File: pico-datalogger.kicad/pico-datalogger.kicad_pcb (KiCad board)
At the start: 2 copper layers, 21 x 33.8 mm, 18 parts, among them J1 JST-PH2 Bat, J2 Pico Pin 1-13, J3 Pico Pin 40-28, J4 Alt-Bat, SW1 SW_Push_SLIM, U1 SN74HC74N, U2 PCF8563T, Y1 Crystal

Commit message: Rev. 0.9: initial routing
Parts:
- removed C3: 22pF, Capacitor_SMD:C_0402_1005Metric
- removed D1: D_Schottky, Diode_SMD:D_SMA
- removed R5: 10K, Resistor_SMD:R_0402_1005Metric
- added BT1: Coin_Cell, user:CR2032_Holder, F.Cu at (165.0, 82.5)
- added J5: Conn_I2S, Connector_PinHeader_2.54mm:PinHeader_1x06_P2.54mm_Vertical, F.Cu at (121.2, 92.3)
- added J7: Micro_SD_TF_PUSH, user:TF-Push, F.Cu at (164.8, 127.7)
- added U3: Pico, user:RPi_Pico_TH_nodbg, F.Cu at (139.2, 94.6)
- J1: value JST-PH2 Bat -> JST-PH2 VCC
- J2: value Pico Pin 1-13 -> Conn_I2C_Internal; footprint user:Connector_1x13_no_solder -> Connector_PinHeader_2.54mm:PinHeader_2x04_P2.54mm_Vertical; moved to F.Cu
- J3: value Pico Pin 40-28 -> RFM9x_Lora_Breakout; footprint user:Connector_1x13_no_solder -> user:RFM9x_Lora_Breakout
- J4: value Alt-Bat -> Alt-VCC
- JP1: value Jmp_CLKOUT -> Jumper_VSYS; footprint Jumper:SolderJumper-2_P1.3mm_Open_Pad1.0x1.5mm -> Connector_PinHeader_2.54mm:PinHeader_1x02_P2.54mm_Vertical; moved to F.Cu
- U2: value PCF8563T -> PCF8523T
- moved J1 67.8 mm to (169.9, 103.1), turned to 90 degrees
- moved J4 62.2 mm to (162.8, 104.3), turned to 0 degrees
- moved JP1 54.0 mm to (152.4, 73.0), turned to 0 degrees
- moved C1 41.5 mm to (136.9, 87.4), turned to 90 degrees
- moved R4 40.4 mm to (133.7, 79.3), turned to 0 degrees
- moved R3 40.1 mm to (133.7, 78.0), turned to 0 degrees
- moved U2 37.6 mm to (138.6, 80.0), turned to 180 degrees
- moved R2 37.2 mm to (132.9, 95.0)
- moved U1 36.9 mm to (138.1, 92.2)
- moved R1 35.7 mm to (133.2, 83.2), turned to 180 degrees
- moved Y1 34.4 mm to (142.3, 84.0), turned to 0 degrees
- moved C2 33.0 mm to (135.9, 83.2), turned to 180 degrees
- moved J2 32.2 mm to (118.5, 67.8), turned to 0 degrees
- moved SW1 31.0 mm to (144.1, 135.3), turned to 180 degrees
- moved J3 28.6 mm to (121.8, 118.6), turned to 90 degrees
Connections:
- J2 pad 1: unconnected-(J2-Pad1) -> GND
- J2 pad 2: unconnected-(J2-Pad2) -> GND
- J2 pad 3: GND -> +3V3
- J2 pad 4: /SDA -> +3V3
- J2 pad 5: /SCL -> /SDA
- J2 pad 6: /GP4_DONE -> /SDA
- J2 pad 7: /GP5_CLKOUT -> /SCL
- J2 pad 8: GND -> /SCL
- J3 pad 1: unconnected-(J3-Pad1) -> +3V3
- J3 pad 11: unconnected-(J3-Pad11) -> (no net)
- J3 pad 12: unconnected-(J3-Pad12) -> (no net)
- J3 pad 13: GND -> (no net)
- J3 pad 2: /VSYS -> GND
- J3 pad 3: GND -> /Lora_EN
- J3 pad 4: /3V3_EN -> unconnected-(J3-Pad4)
- J3 pad 5: +3V3 -> /SCLK1
- J3 pad 6: unconnected-(J3-Pad6) -> /MISO1
- J3 pad 7: unconnected-(J3-Pad7) -> /MOSI1
- J3 pad 8: GND -> /Lora_CS
- J3 pad 9: unconnected-(J3-Pad9) -> /Lora_RST
- JP1 pad 1: /GP5_CLKOUT -> /VSYS
- JP1 pad 2: /CLKOUT -> +BATT
- R3 pad 1: /SCL -> +3V3
- R3 pad 2: +3V3 -> /SDA
- R4 pad 1: /SDA -> +3V3
- R4 pad 2: +3V3 -> /SCL
- U2 pad 3: /1~{PRE} -> Net-(BT1-Pad1)
- U2 pad 7: /CLKOUT -> /1~{PRE}
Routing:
- net +3V3: track 12.8 -> 145.5 mm, vias 1 -> 2
- net /SD_CS: track 0.00 -> 31.4 mm
- net Net-(BT1-Pad1): track 0.00 -> 30.2 mm
- net /DOUT: track 0.00 -> 27.4 mm, vias 0 -> 2
- net GND: track 27.7 -> 1.78 mm, vias 4 -> 0
- net +BATT: track 53.6 -> 77.7 mm, vias 2 -> 1
- net /MOSI0: track 0.00 -> 22.9 mm
- net /SCLK0: track 0.00 -> 19.8 mm
- net /1~{PRE}: track 49.8 -> 69.5 mm
- net /MISO0: track 0.00 -> 14.3 mm
- net /MISO1: track 0.00 -> 13.6 mm
- net /Lora_EN: track 0.00 -> 10.9 mm
- net /SCLK1: track 0.00 -> 10.7 mm
- net /Lora_RST: track 0.00 -> 10.7 mm
- net /MOSI1: track 0.00 -> 9.82 mm
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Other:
- board size 21 x 33.8 mm -> 81 x 90 mm
- board text added: "3V3"
- board text added: "BLCK"
- board text added: "DOUT"
- board text added: "LRCL"
- board text added: "Lora-Breakout"
- board text added: "Pico Inky Pack"
- board text added: "SD-Reader"
- board text removed: "1"
- board text removed: "40"
- board text removed: "C"
- board text removed: "D"
- board text removed: "GP4_DONE"
- board text removed: "GP5_CLKOUT"
- board text removed: "github.com/bablokb/pico-en-control Rev. 3.1"

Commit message: Rev. 0.95: review for production
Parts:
- added H1: MountingHole, MountingHole:MountingHole_2.5mm, F.Cu at (103.0, 53.0)
- added H2: MountingHole, MountingHole:MountingHole_2.5mm, F.Cu at (177.0, 53.0)
- added H3: MountingHole, MountingHole:MountingHole_2.5mm, F.Cu at (103.0, 137.0)
- added H4: MountingHole, MountingHole:MountingHole_2.5mm, F.Cu at (177.0, 137.0)
- added J10: Conn_Inky_SW, Connector_PinHeader_2.54mm:PinHeader_1x03_P2.54mm_Vertical, F.Cu at (131.1, 112.9)
- added J6: Conn_Inky_SPI, Connector_PinHeader_2.54mm:PinHeader_1x08_P2.54mm_Vertical, F.Cu at (157.5, 102.9)
- added J8: Conn_ADC, Connector_PinHeader_2.54mm:PinHeader_1x03_P2.54mm_Horizontal, F.Cu at (169.2, 63.3)
- added J9: Conn_UART, Connector_PinHeader_2.54mm:PinHeader_1x04_P2.54mm_Horizontal, F.Cu at (114.8, 60.7)
- J4: moved to F.Cu
- moved Y1 6.43 mm to (148.7, 83.3), turned to 90 degrees
- moved BT1 5.39 mm to (170.0, 84.5)
- moved C1 5.39 mm to (141.9, 89.4)
- moved C2 5.39 mm to (140.9, 85.2), turned to 0 degrees
- moved J2 5.39 mm to (123.5, 69.8)
- moved J3 5.39 mm to (126.8, 120.6)
- moved J5 5.39 mm to (126.2, 94.3)
- moved JP1 5.39 mm to (157.4, 75.0)
- moved R1 5.39 mm to (138.2, 85.2)
- moved R2 5.39 mm to (137.9, 97.0)
- moved R3 5.39 mm to (138.7, 80.0)
- moved R4 5.39 mm to (138.7, 81.3)
- moved SW1 5.39 mm to (149.1, 137.3)
- moved U1 5.39 mm to (143.1, 94.2)
- moved U2 5.39 mm to (143.6, 82.0)
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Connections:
- U3 pad 1: unconnected-(U3-Pad1) -> /TX
- U3 pad 2: unconnected-(U3-Pad2) -> /RX
- U3 pad 32: unconnected-(U3-Pad32) -> /GP27_ADC1
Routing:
- net +3V3: track 145.5 -> 181.9 mm, vias 2 -> 3
- net /GP27_ADC1: track 0.00 -> 34.0 mm
- net /RX: track 0.00 -> 26.5 mm
- net /TX: track 0.00 -> 22.8 mm
- net /Inky_RUN: track 0.00 -> 9.44 mm
- net /Inky_BUSY: track 0.00 -> 9.44 mm
- net /Inky_DC: track 0.00 -> 5.50 mm
- net /Inky_RST: track 0.00 -> 5.50 mm
- net /Inky_SWB: track 0.00 -> 5.14 mm
- net /Inky_SWA: track 0.00 -> 5.14 mm
- net /MISO0: track 14.3 -> 9.31 mm
- net /Inky_CS: track 0.00 -> 4.47 mm
- net /Inky_SWC: track 0.00 -> 4.24 mm
- net /SCLK0: track 19.8 -> 16.3 mm
- net /MOSI0: track 22.9 -> 19.8 mm
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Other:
- board size 81 x 90 mm -> 80 x 90 mm
- board text added: "GP27/ADC1"
- board text added: "I-BSY"
- board text added: "I-RST"
- board text added: "I-RUN"
- board text added: "Inky-CS"
- board text added: "Inky-DC"
- board text added: "MISO"
- board text added: "MOSI"
- board text added: "RX"
- board text added: "SCLK"
- board text added: "SWA"
- board text added: "SWC"
- board text added: "TX"
- board text added: "https://github.com/bablokb/pcb-pico-datalogger https://opendeved.net Rev 0.95"

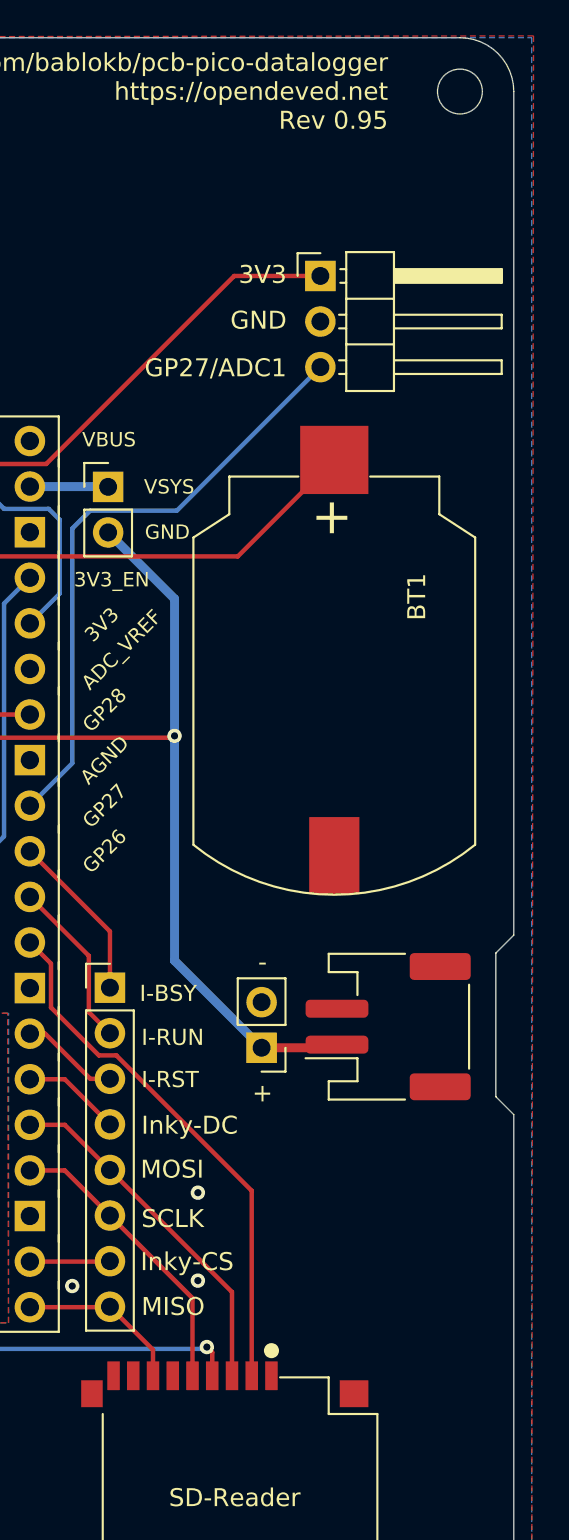
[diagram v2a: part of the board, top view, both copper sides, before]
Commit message: Rev 0.96: added reset-button
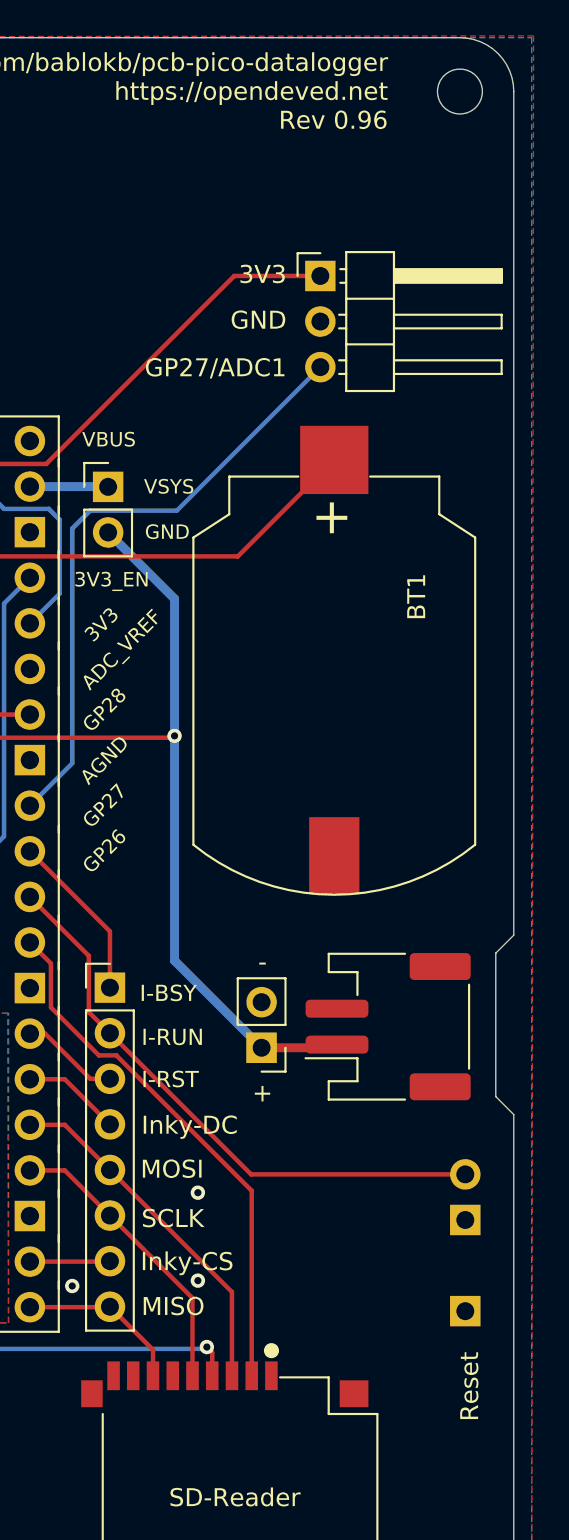
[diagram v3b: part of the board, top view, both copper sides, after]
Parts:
- added SW2: SW_Reset, user:SW_PUSH_SLIM_1x4, F.Cu at (177.3, 121.0)
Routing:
- net /Inky_RUN: track 9.44 -> 32.5 mm
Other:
- board text added: "Reset"
- board text added: "https://github.com/bablokb/pcb-pico-datalogger https://opendeved.net Rev 0.96"
- board text removed: "https://github.com/bablokb/pcb-pico-datalogger https://opendeved.net Rev 0.95"
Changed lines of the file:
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@@
     )
+  )
+  (footprint "user:SW_PUSH_SLIM_1x4" (layer "F.Cu")
+    (at 177.3 120.95 90)
+    (descr "Slim Pushbutton")
+    (tags "connector")
+    (property "Sheetfile" "pico-datalogger.kicad_sch")
+    (property "Sheetname" "")
+    (attr exclude_from_pos_files)
+    (fp_text reference "SW2" (at 1.27 -3.175 90) (layer "F.SilkS") hide
+      (effects (font (size 1 1) (thickness 0.15)))
+    )
+    (fp_text value "SW_Reset" (at 3.73126 2.92608 90) (layer "F.Fab")
+      (effects (font (size 1 1) (thickness 0.15)))
+    )
+    (fp_text user "${REFERENCE}" (at 1.27 1.27 90) (layer "F.Fab")
+      (effects (font (size 1 1) (thickness 0.15)))
+    )
+    (fp_line (start -1.27 -1.8) (end 8.89 -1.8) (layer "F.CrtYd") (width 0.05))
+    (fp_line (start -1.27 -1.8) (end -1.27 1.8) (layer "F.CrtYd") (width 0.05))
+    (fp_line (start -1.27 1.8) (end 8.89 1.8) (layer "F.CrtYd") (width 0.05))
+    (fp_line (start 8.89 -1.8) (end 8.89 1.8) (layer "F.CrtYd") (width 0.05))
+    (pad "1" thru_hole rect (at 5.08 0 90) (size 1.7 1.7) (drill 1) (layers *.Cu *.Mask)
+      (net 2 "GND") (pinfunction "1") (pintype "passive"))
+    (pad "1" thru_hole rect (at 0 0 90) (size 1.7 1.7) (drill 1) (layers *.Cu *.Mask)
+      (net 2 "GND") (pinfunction "1") (pintype "passive"))
+    (pad "2" thru_hole circle (at 7.62 0 90) (size 1.7 1.7) (drill 1) (layers *.Cu *.Mask)
+      (net 42 "/Inky_RUN") (pinfunction "2") (pintype "passive"))
   )
   (footprint "Resistor_SMD:R_0402_1005Metric" (layer "F.Cu")
@@
     (effects (font (size 1 1) (thickness 0.15)) (justify left mirror))
   )
+  (gr_text "Reset" (at 177.55 125.15 90) (layer "B.SilkS")
+    (effects (font (size 1 1) (thickness 0.15)) (justify mirror))
+  )
   (gr_text "-" (at 166 101.65 180) (layer "B.SilkS")
     (effects (font (size 1 1) (thickness 0.15)) (justify mirror))
@@
     (effects (font (size 1 1) (thickness 0.15)))
   )
+  (gr_text "Reset" (at 177.55 125.15 90) (layer "F.SilkS")
+    (effects (font (size 1 1) (thickness 0.15)))
+  )
   (gr_text "DOUT" (at 124.2 89.1) (layer "F.SilkS")
     (effects (font (size 1 1) (thickness 0.15)) (justify right))
@@
     (effects (font (size 1 1) (thickness 0.15)) (justify right))
   )
-  (gr_text "https://github.com/bablokb/pcb-pico-datalogger\nhttps://opendeved.net\nRev 0.95" (at 173 53) (layer "F.SilkS")
+  (gr_text "https://github.com/bablokb/pcb-pico-datalogger\nhttps://opendeved.net\nRev 0.96" (at 173 53) (layer "F.SilkS")
     (effects (font (size 1 1) (thickness 0.15)) (justify right))
   )
@@
   (segment (start 153.04 105.49) (end 153.89 105.49) (width 0.25) (layer "F.Cu") (net 41))
   (segment (start 153.04 97.87) (end 156.325 101.155) (width 0.25) (layer "F.Cu") (net 42))
+  (segment (start 157.5 105.465) (end 165.365 113.33) (width 0.25) (layer "F.Cu") (net 42))
   (segment (start 156.325 101.155) (end 156.325 104.29) (width 0.25) (layer "F.Cu") (net 42))
   (segment (start 156.325 104.29) (end 157.5 105.465) (width 0.25) (layer "F.Cu") (net 42))
+  (segment (start 165.365 113.33) (end 177.3 113.33) (width 0.25) (layer "F.Cu") (net 42))
   (segment (start 153.04 95.33) (end 157.5 99.79) (width 0.25) (layer "F.Cu") (net 43))
   (segment (start 157.5 99.79) (end 157.5 102.925) (width 0.25) (layer "F.Cu") (net 43))
@@
     (polygon
       (pts
+        (xy 150 85.55)
+        (xy 139.8 85.55)
+        (xy 139.8 79.05)
+        (xy 150 79.05)
+      )
+    )
+  )
+  (zone (net 2) (net_name "GND") (layer "B.Cu") (hatch edge 0.508)
+    (connect_pads (clearance 0.508))
+    (min_thickness 0.254) (filled_areas_thickness no)
+    (fill yes (thermal_gap 0.508) (thermal_bridge_width 0.508))
+    (polygon
+      (pts
         (xy 181 140)
         (xy 100 140)
@@
       )
     )
-  )
-  (zone (net 2) (net_name "GND") (layer "B.Cu") (hatch edge 0.508)
-    (connect_pads (clearance 0.508))
-    (min_thickness 0.254) (filled_areas_thickness no)
-    (fill yes (thermal_gap 0.508) (thermal_bridge_width 0.508))
-    (polygon
-      (pts
-        (xy 150 85.55)
-        (xy 139.8 85.55)
-        (xy 139.8 79.05)
-        (xy 150 79.05)
-      )
-    )

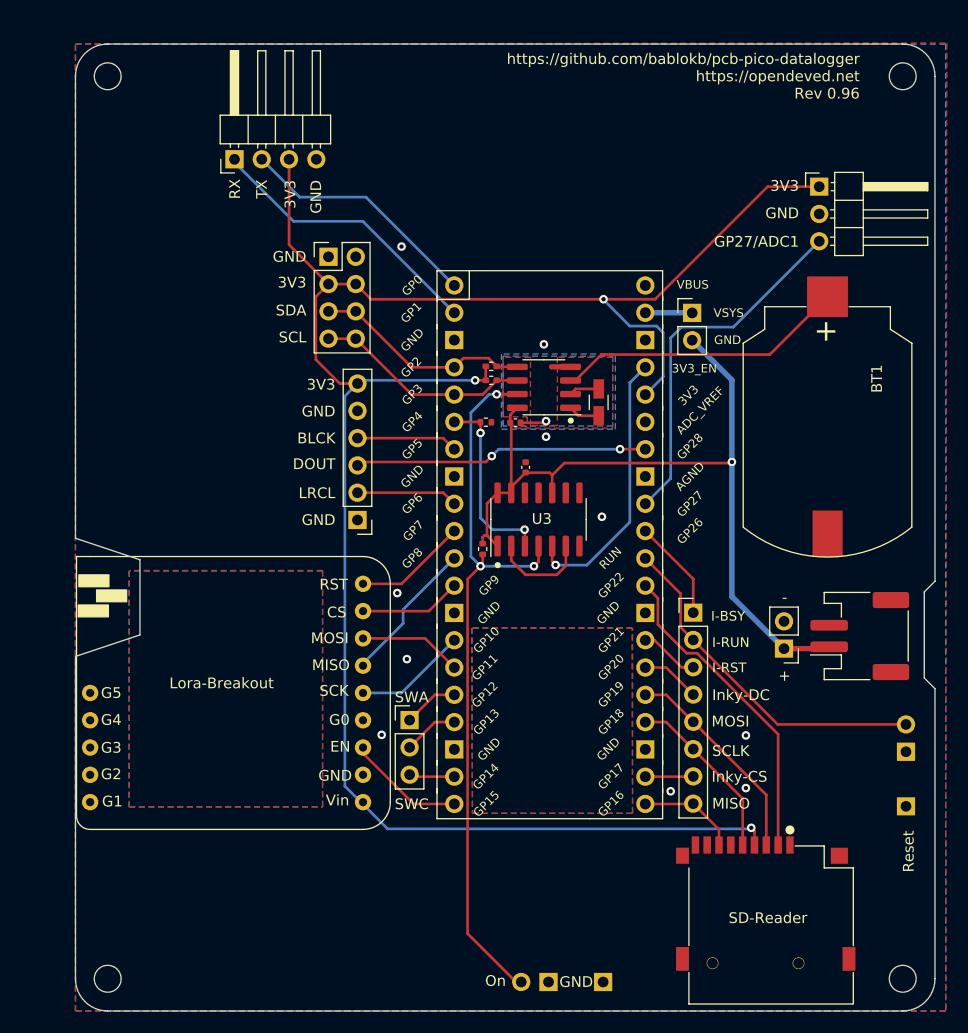
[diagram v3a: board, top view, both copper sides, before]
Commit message: fix: added 3V3 and GND for InkyPack-connector
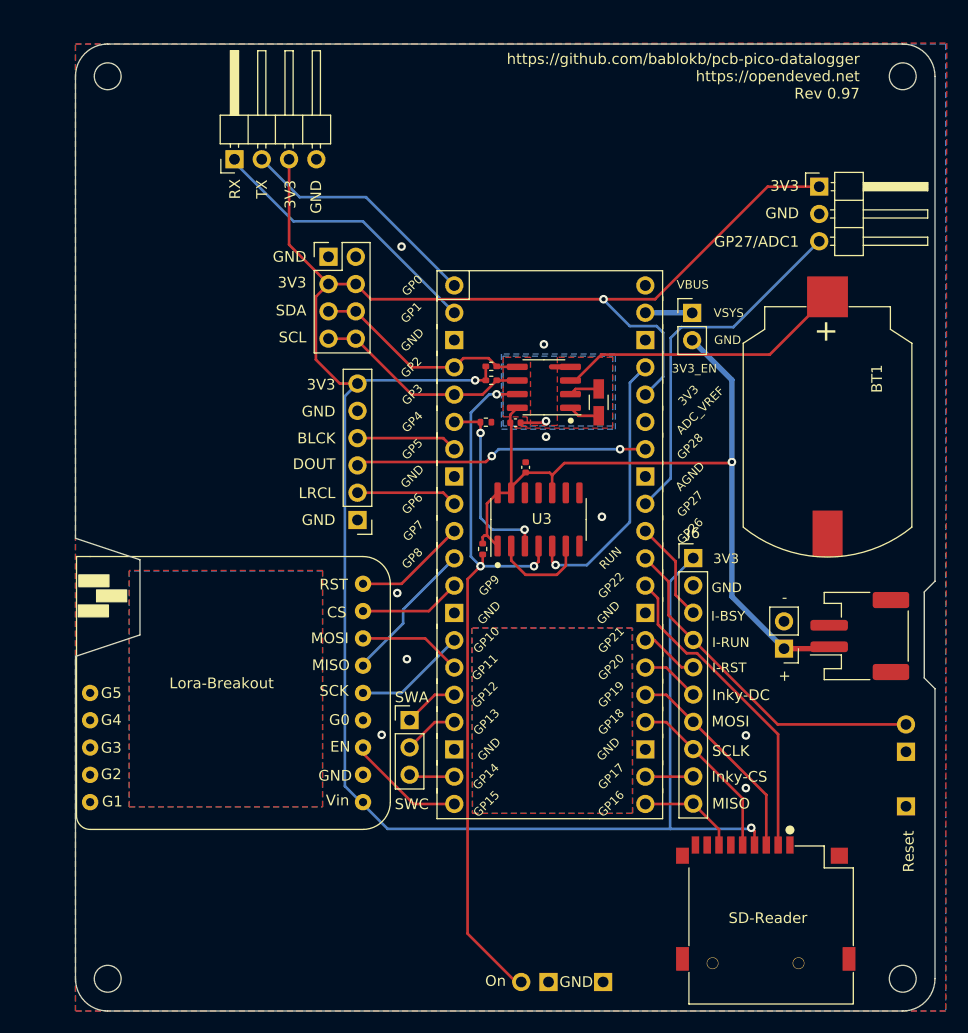
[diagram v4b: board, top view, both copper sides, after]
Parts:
- J6: footprint Connector_PinHeader_2.54mm:PinHeader_1x08_P2.54mm_Vertical -> Connector_PinHeader_2.54mm:PinHeader_1x10_P2.54mm_Vertical
- moved J6 5.08 mm to (157.5, 97.8)
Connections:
- J6 pad 1: /Inky_BUSY -> +3V3
- J6 pad 2: /Inky_RUN -> GND
- J6 pad 3: /Inky_RST -> /Inky_BUSY
- J6 pad 4: /Inky_DC -> /Inky_RUN
- J6 pad 5: /MOSI0 -> /Inky_RST
- J6 pad 6: /SCLK0 -> /Inky_DC
- J6 pad 7: /Inky_CS -> /MOSI0
- J6 pad 8: /MISO0 -> /SCLK0
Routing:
- net +3V3: track 181.9 -> 208.0 mm
- net GND: vias 11 -> 10
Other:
- board text added: "https://github.com/bablokb/pcb-pico-datalogger https://opendeved.net Rev 0.97"
- board text removed: "https://github.com/bablokb/pcb-pico-datalogger https://opendeved.net Rev 0.96"
